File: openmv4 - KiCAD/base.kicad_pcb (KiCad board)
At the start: 4 copper layers, 35.6 x 44.5 mm, 55 parts, among them M1 9774030243R, M2 9774030243R, Q1 BSS138, Q2 Si2301BDS, U1 STM32H743VIT6, U5 TPS731XX, U8 PAM2305AABADJ, X1 MF-CON-MICROUSB-RIGHT, X2 USD-1040310811, X3 DF12-36-DS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

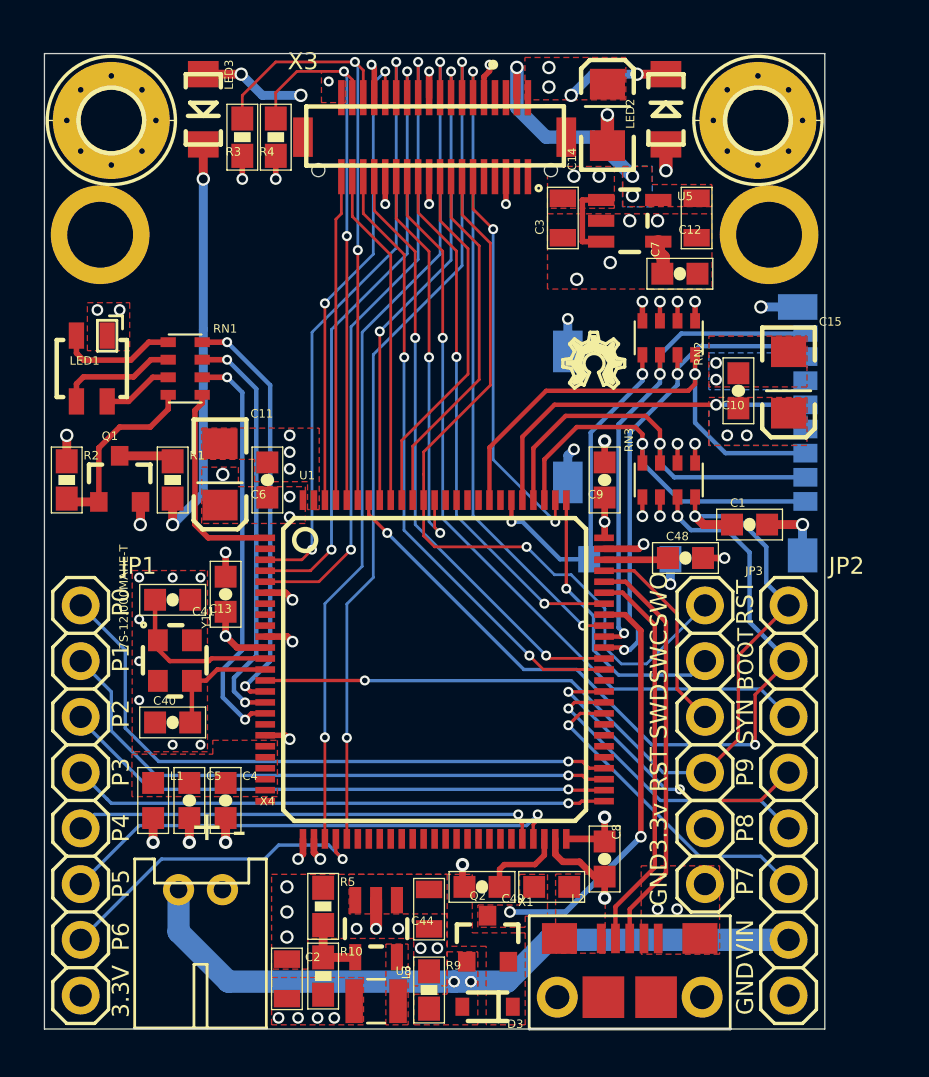
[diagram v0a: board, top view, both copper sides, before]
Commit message: Cleaned Schematic, Moved USB, Added Pin Socket
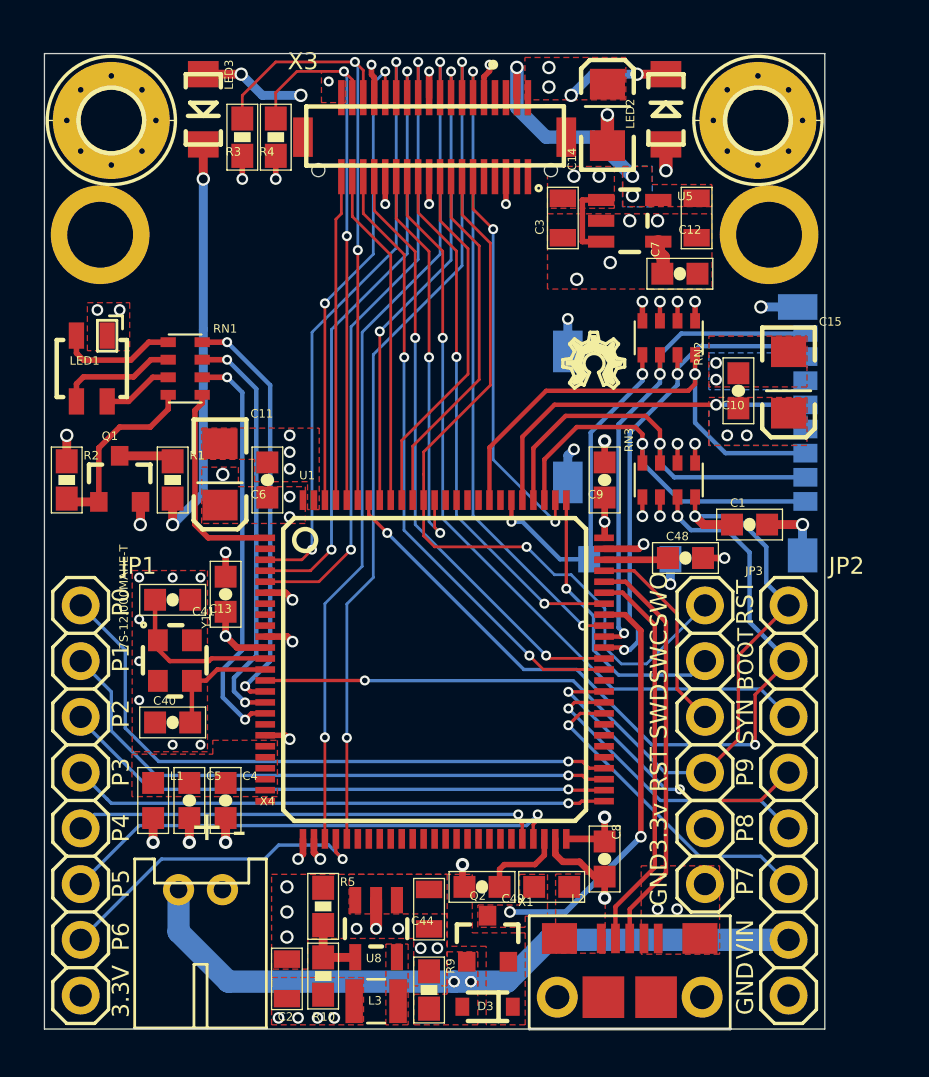
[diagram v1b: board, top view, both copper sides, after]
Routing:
- added copper zone on In1.Cu, net GND
- added copper zone on In2.Cu, net VCC
- removed copper zone on GND, net GND
- removed copper zone on VCC, net VCC
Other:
- net class Default removed
